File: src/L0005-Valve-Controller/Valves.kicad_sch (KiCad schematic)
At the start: 53 parts, among them K1 AQH0223AX, K2 AQH0223AX, K3 AQH0223AX, K4 AQH0223AX, K5 AQH0223AX, K6 AQH0223AX, P10 353620650, P11 353620650, P12 353620650, P13 353620650, P14 647676-3, P15 647676-3, P3 647676-3, P4 647676-3, P5 647676-3, P6 647676-3, P7 647676-3, P8 647676-3, Q1 CMLDM7003, Q2 CMLDM7003, Q3 CMLDM7003

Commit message: routed rev3
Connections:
- net SBV1_PUL: now also Q3.4 (G); no longer Q3.1 (G)
- net SBV1_PUL-: now also Q3.3 (D); no longer Q3.6 (D)
- net SBV2_PUL: now also Q3.1 (G); no longer Q3.4 (G)
- net SBV2_PUL-: now also Q3.6 (D); no longer Q3.3 (D)
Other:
- moved on the sheet: Q3A, Q3B
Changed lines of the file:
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@@
     )
   )
-  (symbol (lib_id "L0005-Valve-Controller:CMLDM7003") (at 195.58 134.874 0) (unit 2)
+  (symbol (lib_id "L0005-Valve-Controller:CMLDM7003") (at 197.358 76.962 0) (unit 2)
     (in_bom yes) (on_board yes) (dnp no)
-    (property "Reference" "Q3" (at 191.262 131.826 0)
+    (property "Reference" "Q3" (at 193.04 73.914 0)
       (effects (font (size 1.27 1.27)) (justify left))
     )
-    (property "Value" "CMLDM7003" (at 200.66 134.874 0)
+    (property "Value" "CMLDM7003" (at 202.438 76.962 0)
       (effects (font (size 1.27 1.27)) (justify left) hide)
     )
-    (property "Footprint" "L0005-Valve-Controller:CMLDM7003 TR" (at 201.676 142.748 0)
+    (property "Footprint" "L0005-Valve-Controller:CMLDM7003 TR" (at 203.454 84.836 0)
       (effects (font (size 1.27 1.27) italic) (justify left) hide)
     )
-    (property "Datasheet" "https://www.onsemi.com/pub/Collateral/NDS7002A-D.PDF" (at 194.31 138.176 0)
+    (property "Datasheet" "https://www.onsemi.com/pub/Collateral/NDS7002A-D.PDF" (at 196.088 80.264 0)
       (effects (font (size 1.27 1.27)) (justify left) hide)
     )
@@
     )
   )
-  (symbol (lib_id "L0005-Valve-Controller:CMLDM7003") (at 197.358 76.962 0) (unit 1)
+  (symbol (lib_id "L0005-Valve-Controller:CMLDM7003") (at 195.58 134.874 0) (unit 1)
     (in_bom yes) (on_board yes) (dnp no)
-    (property "Reference" "Q3" (at 193.294 73.66 0)
+    (property "Reference" "Q3" (at 191.516 131.572 0)
       (effects (font (size 1.27 1.27)) (justify left))
     )
-    (property "Value" "CMLDM7003" (at 202.438 76.962 0)
+    (property "Value" "CMLDM7003" (at 200.66 134.874 0)
       (effects (font (size 1.27 1.27)) (justify left) hide)
     )
-    (property "Footprint" "L0005-Valve-Controller:CMLDM7003 TR" (at 203.454 84.836 0)
+    (property "Footprint" "L0005-Valve-Controller:CMLDM7003 TR" (at 201.676 142.748 0)
       (effects (font (size 1.27 1.27) italic) (justify left) hide)
     )
-    (property "Datasheet" "https://www.onsemi.com/pub/Collateral/NDS7002A-D.PDF" (at 196.088 80.264 0)
+    (property "Datasheet" "https://www.onsemi.com/pub/Collateral/NDS7002A-D.PDF" (at 194.31 138.176 0)
       (effects (font (size 1.27 1.27)) (justify left) hide)
     )

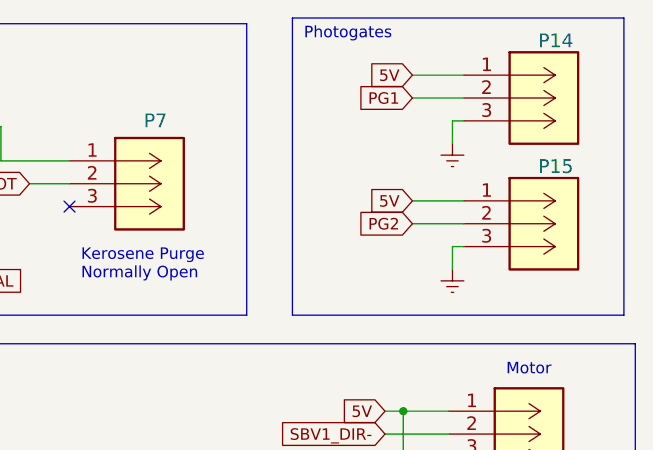
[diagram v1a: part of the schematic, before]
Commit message: fixed photogate pinouts to allow for straight cable to photogate connector
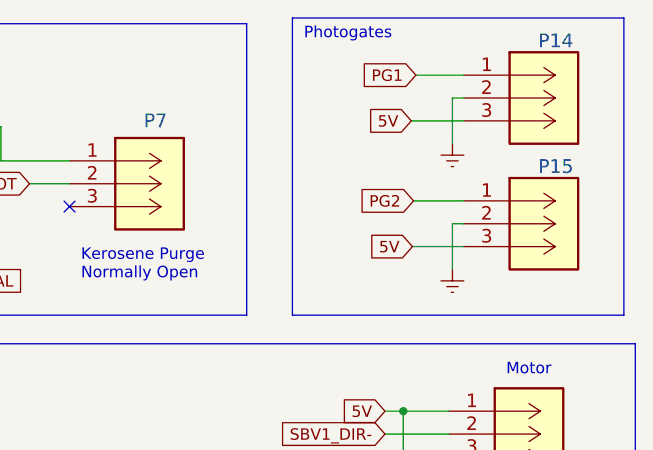
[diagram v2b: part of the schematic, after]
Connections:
- net 5V: now also P14.3, P15.3; no longer P14.1, P15.1
- net Earth: now also P14.2, P15.2; no longer P14.3, P15.3
- net PG1: now also P14.1; no longer P14.2
- net PG2: now also P15.1; no longer P15.2
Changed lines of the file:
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@@
-    (stroke (width 0) (type default))
-  )
-  (wire (pts (xy 234.95 21.59) (xy 240.665 21.59))
     (stroke (width 0) (type default))
   )
@@
     (stroke (width 0) (type default))
   )
+  (wire (pts (xy 240.665 24.13) (xy 239.395 24.13))
+    (stroke (width 0) (type default))
+  )
   (wire (pts (xy 230.886 129.54) (xy 238.76 129.54))
     (stroke (width 0) (type default))
@@
     (stroke (width 0) (type default))
   )
+  (wire (pts (xy 240.665 26.67) (xy 234.823 26.67))
+    (stroke (width 0) (type default))
+  )
   (polyline (pts (xy 125.73 160.655) (xy 125.73 107.95))
     (stroke (width 0) (type default))
@@
     (stroke (width 0) (type default))
   )
-  (wire (pts (xy 234.95 35.56) (xy 240.665 35.56))
-    (stroke (width 0) (type default))
-  )
   (wire (pts (xy 57.785 170.815) (xy 53.34 170.815))
     (stroke (width 0) (type default))
@@
     (stroke (width 0) (type default))
   )
-  (wire (pts (xy 239.395 26.67) (xy 240.665 26.67))
-    (stroke (width 0) (type default))
-  )
   (wire (pts (xy 56.515 61.595) (xy 67.31 61.595))
     (stroke (width 0) (type default))
@@
     (stroke (width 0) (type default))
   )
-  (wire (pts (xy 234.95 38.1) (xy 240.665 38.1))
-    (stroke (width 0) (type default))
-  )
   (wire (pts (xy 215.265 139.7) (xy 220.345 139.7))
     (stroke (width 0) (type default))
@@
     (stroke (width 0) (type default))
   )
+  (wire (pts (xy 239.395 43.18) (xy 239.395 38.1))
+    (stroke (width 0) (type default))
+  )
   (wire (pts (xy 236.855 151.13) (xy 236.855 149.86))
     (stroke (width 0) (type default))
@@
     (stroke (width 0) (type default))
   )
-  (wire (pts (xy 239.395 43.18) (xy 239.395 40.64))
-    (stroke (width 0) (type default))
-  )
   (wire (pts (xy 81.915 25.4) (xy 81.915 29.21))
     (stroke (width 0) (type default))
@@
     (stroke (width 0) (type default))
   )
+  (wire (pts (xy 235.331 21.59) (xy 240.665 21.59))
+    (stroke (width 0) (type default))
+  )
   (wire (pts (xy 163.83 27.305) (xy 159.385 27.305))
     (stroke (width 0) (type default))
@@
     (stroke (width 0) (type default))
   )
-  (wire (pts (xy 239.395 40.64) (xy 240.665 40.64))
-    (stroke (width 0) (type default))
-  )
   (polyline (pts (xy 259.715 107.95) (xy 259.715 160.655))
     (stroke (width 0) (type default))
@@
     (stroke (width 0) (type default))
   )
+  (wire (pts (xy 235.077 35.56) (xy 240.665 35.56))
+    (stroke (width 0) (type default))
+  )
   (wire (pts (xy 83.185 174.625) (xy 90.805 174.625))
     (stroke (width 0) (type default))
@@
     (stroke (width 0) (type default))
   )
-  (wire (pts (xy 234.95 24.13) (xy 240.665 24.13))
-    (stroke (width 0) (type default))
-  )
   (wire (pts (xy 173.99 67.818) (xy 173.99 72.39))
     (stroke (width 0) (type default))
@@
     (stroke (width 0) (type default))
   )
+  (wire (pts (xy 234.95 40.64) (xy 240.665 40.64))
+    (stroke (width 0) (type default))
+  )
   (wire (pts (xy 67.31 25.4) (xy 81.915 25.4))
     (stroke (width 0) (type default))
@@
     (stroke (width 0) (type default))
   )
+  (wire (pts (xy 239.395 38.1) (xy 240.665 38.1))
+    (stroke (width 0) (type default))
+  )
   (polyline (pts (xy 20.32 155.575) (xy 20.32 123.19))
     (stroke (width 0) (type default))
@@
     (stroke (width 0) (type default))
   )
-  (wire (pts (xy 239.395 29.21) (xy 239.395 26.67))
-    (stroke (width 0) (type default))
-  )
   (polyline (pts (xy 20.32 83.82) (xy 20.32 50.8))
     (stroke (width 0) (type default))
   )
   (wire (pts (xy 174.625 27.305) (xy 189.23 27.305))
+    (stroke (width 0) (type default))
+  )
+  (wire (pts (xy 239.395 24.13) (xy 239.395 29.21))
     (stroke (width 0) (type default))
   )
@@
     )
   )
-  (global_label "PG1" (shape input) (at 234.95 24.13 180) (fields_autoplaced)
-    (effects (font (size 1.27 1.27)) (justify right))
-    (property "Intersheetrefs" "${INTERSHEET_REFS}" (at 80.01 -29.21 0)
-      (effects (font (size 1.27 1.27)) hide)
-    )
-  )
-  (global_label "5V" (shape input) (at 234.95 35.56 180) (fields_autoplaced)
-    (effects (font (size 1.27 1.27)) (justify right))
-    (property "Intersheetrefs" "${INTERSHEET_REFS}" (at 80.01 -29.21 0)
+  (global_label "PG1" (shape input) (at 235.331 21.59 180) (fields_autoplaced)
+    (effects (font (size 1.27 1.27)) (justify right))
+    (property "Intersheetrefs" "${INTERSHEET_REFS}" (at 80.391 -31.75 0)
+      (effects (font (size 1.27 1.27)) hide)
+    )
+  )
+  (global_label "5V" (shape input) (at 234.95 40.64 180) (fields_autoplaced)
+    (effects (font (size 1.27 1.27)) (justify right))
+    (property "Intersheetrefs" "${INTERSHEET_REFS}" (at 80.01 -24.13 0)
       (effects (font (size 1.27 1.27)) hide)
     )
@@
     )
   )
-  (global_label "5V" (shape input) (at 234.95 21.59 180) (fields_autoplaced)
-    (effects (font (size 1.27 1.27)) (justify right))
-    (property "Intersheetrefs" "${INTERSHEET_REFS}" (at 80.01 -29.21 0)
+  (global_label "5V" (shape input) (at 234.823 26.67 180) (fields_autoplaced)
+    (effects (font (size 1.27 1.27)) (justify right))
+    (property "Intersheetrefs" "${INTERSHEET_REFS}" (at 79.883 -24.13 0)
       (effects (font (size 1.27 1.27)) hide)
     )
@@
     )
   )
-  (global_label "PG2" (shape input) (at 234.95 38.1 180) (fields_autoplaced)
-    (effects (font (size 1.27 1.27)) (justify right))
-    (property "Intersheetrefs" "${INTERSHEET_REFS}" (at 80.01 -29.21 0)
-      (effects (font (size 1.27 1.27)) hide)
-    )
+  (global_label "PG2" (shape input) (at 235.077 35.56 180) (fields_autoplaced)
+    (effects (font (size 1.27 1.27)) (justify right))
+    (property "Intersheetrefs" "${INTERSHEET_REFS}" (at 80.137 -31.75 0)
+      (effects (font (size 1.27 1.27)) hide)
+    )
